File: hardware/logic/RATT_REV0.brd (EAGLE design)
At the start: 127 x 76.2 mm, 126 parts, among them IC1 TLP292-4, IC13 MCP73832, IC16 PCA9539PW, IC2 CPC1002N, IC200 TPS2115AIPWRQ1, IC3 CPC1002N, IC300 MAx98357, IC4 CPC1002N, IC5 CPC1002N, J1 4P-2.0, J2 4P-2.0, J4 4P-2.0, J5 F-1X04-SIP-100-40, J6 4P-2.0, J7 PHOENIX1803484, J8 PHOENIX1803484, Q5 2N7002, U1 RPI-ZERO, U5 AP2112K-3.3V

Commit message: Moved all parts into MakeItLabs Library
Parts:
- removed U5: AP2112K-3.3V, SparkFun-PowerIC:SOT23-5
- added IC500: AP2112K-3.3V, MakeItLabs:SOT23-5
- C1, C20, C23: device SparkFun-Capacitors:0805@1 -> MakeItLabs:0805-CAP
- C10, C19, C8: device SparkFun-Capacitors:0603 -> MakeItLabs:0603-CAP
- C18, C2, C22, C3: device SparkFun-Capacitors:0603-CAP@1 -> MakeItLabs:0603-CAP
- C7: device SparkFun-Capacitors:0805 -> MakeItLabs:0603-CAP
- D10, D2, D3, D5, D6, D7, D8, D9: device DURRIDGE-DIODES:SOT-23 -> MakeItLabs:SOT-23
- FB1, FB2: device Adafruit_MAX98357:0603 -> MakeItLabs:0603
- FB3, FB4: device DURRIDGE-INDUCTORS:0603 -> MakeItLabs:0603
- IC1: device DURRIDGE-IC:SO-16 -> MakeItLabs:SO-16
- IC13: device SparkFun-PowerIC:SOT23-5 -> MakeItLabs:SOT23-5
- IC16: device Texas Instruments_By_element14_Batch_1:SOP65P640X120-24N -> MakeItLabs:SOP65P640X120-24N
- IC200: device Texas Instruments_By_element14_Batch_1:SOP65P640X120-8N -> MakeItLabs:SOP65P640X120-8N
- IC300: value MAx98357 -> MAX98357; device Adafruit_MAX98357:QFN16_3MM -> MakeItLabs:QFN16_3MM
- J100, J200: device Adafruit_MAX98357:TERMBLOCK_1X2-3.5MM -> MakeItLabs:TERMBLOCK_1X2-3.5MM
- J5: device con-headers-jp:SIP-100-04-40 -> MakeItLabs:SIP-100-04-40
- JP1: device pinhead:2X08 -> MakeItLabs:2X08
- JP2: device SparkFun-Connectors:JST-2-PTH -> MakeItLabs:JST-2-PTH
- LED1, LED2: device SparkFun-LED:LED5MM -> MakeItLabs:LED5MM
- LED3, LED4, LED5, LED6: device SparkFun-LED:LED-0603 -> MakeItLabs:LED-0603
- Q5: device zetex:SOT-23 -> MakeItLabs:SOT-23
- R1: device SparkFun-Passives:0603-RES -> MakeItLabs:0603-RES
- R11, R12, R18, R19, R21, R24, R36, R56, R57, R60, R61: device SparkFun-Resistors:0603 -> MakeItLabs:0603-RES
- R14, R15, R16, R22: device DURRIDGE-RESISTORS:2512-RES -> MakeItLabs:2512-RES
- SW0, SW1, SW2, SW3: device MakeIt_Labs:ESWITCH320 -> MakeItLabs:ESWITCH320
- U1: device RPI-Zero:RASPBERRYPI_BASTELSTUBE_V13_RASPI_BOARD_B+_FULL -> MakeItLabs:RASPBERRYPI_BASTELSTUBE_V13_RASPI_BOARD_B+_FULL
- moved R60 146.9 mm to (-78.2, -10.4)
- moved C2 146.9 mm to (-78.2, -16.8)
- moved C3 146.9 mm to (-78.2, -19.8)
- moved R11 146.9 mm to (-75.2, -0.51)
- moved R12 146.9 mm to (-75.2, -3.81)
- moved R61 146.9 mm to (-78.2, -13.7)
- moved IC200 112.7 mm to (-76.2, -27.4)
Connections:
- net +3.3V: now also IC500.5; no longer U5.5
- net +5VB: now also IC500.1; no longer U5.1
- net GND: now also IC500.2; no longer U5.2
- net N$18: now also IC500.3; no longer U5.3
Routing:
- net N$33: track 4.84 -> 6.13 mm
- net N$34: track 4.27 -> 3.29 mm

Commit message: most stuff placed
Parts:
- moved R24 148.9 mm to (45.2, 38.6), turned to 180 degrees
- moved LED5 131.4 mm to (4.32, 51.3)
- moved R57 125.7 mm to (4.32, 48.5), turned to 90 degrees
- moved LED4 125.0 mm to (2.54, 51.3)
- moved R56 119.2 mm to (2.54, 48.5), turned to 90 degrees
- moved C10 119.1 mm to (41.9, 43.9), turned to 180 degrees
- moved R61 115.0 mm to (19.8, 46.5)
- moved LED3 107.3 mm to (6.10, 51.3)
- moved R21 106.9 mm to (6.10, 48.5), turned to 90 degrees
- moved IC200 106.8 mm to (7.37, 39.1), turned to 270 degrees
- moved C2 101.6 mm to (9.65, 34.3)
- moved C7 100.2 mm to (42.7, 39.4), turned to 270 degrees
- moved C3 99.8 mm to (5.59, 34.3), turned to 180 degrees
- moved R60 98.2 mm to (4.57, 42.4)
- moved LED6 98.2 mm to (6.10, 7.62)
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- renumbered U1 to J87
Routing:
- net +5VIN: track 0.00 -> 253.2 mm, vias 0 -> 1
- net +5VB: track 116.6 -> 237.8 mm, vias 8 -> 10
- net CHARGE_STATUS: track 0.00 -> 66.1 mm, vias 0 -> 2
- net SHUTDOWN: track 5.25 -> 50.5 mm, vias 0 -> 2
- net V_BATT: track 0.00 -> 30.5 mm
- net !PWR_LOSS: track 0.00 -> 17.2 mm
- net +3.3V: track 105.2 -> 116.1 mm
- net I2S_WS/LRCLK: track 11.8 -> 16.5 mm
- net I2S_BCK: track 42.6 -> 46.7 mm
- net 3V3: track 23.9 -> 26.9 mm
- net N$18: track 0.00 -> 2.08 mm
- net N$14: track 0.00 -> 1.69 mm
- net I2C_SDA: track 48.5 -> 46.9 mm
- net N$17: track 0.00 -> 1.55 mm
- net I2S_DOUT: track 10.7 -> 9.20 mm
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
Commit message: Added some stuff
Added clamps to RFID, added 1206 series resistor to LCD backlight
power in connector updated
lipo connector moved
played with cut away of plane
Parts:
- removed SJ4: JUMPER-PAD-2-NC_BY_TRACE, MakeItLabs:SOLDERJUMPER_10MIL
- added D1, D4: BAT54S, MakeItLabs:SOT-23
- added R10: 100R, MakeItLabs:0603-RES
- added R9: 10R, MakeItLabs:1206-RES
- J100: value (none) -> PHOENIX1803426; device MakeItLabs:TERMBLOCK_1X2-3.5MM -> MakeItLabs:1803426
- moved C22 34.2 mm to (67.6, 65.2), turned to 90 degrees
- moved C23 32.5 mm to (65.4, 65.3), turned to 90 degrees
- moved FB3 18.7 mm to (66.5, 71.4), turned to 270 degrees
- moved C1 7.90 mm to (48.8, 72.1), turned to 270 degrees
- moved R41 5.74 mm to (72.1, 66.6), turned to 270 degrees
- moved C25 5.65 mm to (50.6, 72.2), turned to 270 degrees
- moved JP2 4.89 mm to (10.7, 19.8), turned to 270 degrees
- moved FB4 4.44 mm to (46.7, 72.1), turned to 270 degrees
- moved R37 3.39 mm to (56.4, 67.6), turned to 90 degrees
- moved R25 2.90 mm to (61.0, 39.9), turned to 90 degrees
- moved R30 2.30 mm to (61.0, 43.2), turned to 270 degrees
- moved R20 2.30 mm to (57.9, 69.1)
- moved J5 1.78 mm to (56.9, 72.1)
- moved R36 1.02 mm to (26.7, 55.9)
- moved LED3 0.51 mm to (6.10, 51.8)
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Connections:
- removed net N$26: LCD3.15, LCD3.2, SJ4.1
- new net N$10: J5.4, R10.2
- new net N$9: LCD3.15, R9.2
- net +3.3V: now also LCD3.2, R9.1; no longer SJ4.2
- net +5VB: now also D1.2, D4.2
- net +5VIN: now also J100.2; no longer J100.1
- net GND: now also D1.1, D4.1, J100.1; no longer J100.2
- net RFID_RX: now also D4.3, R10.1; no longer J5.4
- net RFID_TX: now also D1.3
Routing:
- net +3.3V: track 116.1 -> 296.3 mm, vias 7 -> 17
- net N$26: track 36.2 -> 0.00 mm
- net +5VB: track 237.8 -> 269.6 mm, vias 10 -> 12
- net N$51: track 0.00 -> 24.6 mm
- net !I/O_RESET: track 34.7 -> 29.4 mm, vias 0 -> 2
- net LED0: track 35.6 -> 40.4 mm
- net N$10: track 0.00 -> 4.39 mm
- net +5VIN: track 253.2 -> 256.3 mm
- net CHARGE_STATUS: track 66.1 -> 69.1 mm
- net RFID_TX: track 70.8 -> 73.2 mm
- net I2C_SDA: track 46.9 -> 48.9 mm
- net N$9: track 0.00 -> 1.90 mm
- net LED1: track 39.9 -> 38.8 mm
- net !BUTTON0: track 20.8 -> 21.8 mm
- net !I/O_IRQ: track 32.4 -> 32.7 mm, vias 0 -> 2
- added copper zone on layer 1, net +5VB
- added copper zone on layer 1, net N$16
- removed copper zone on layer 1, net VIN

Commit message: moved stuff for Steve
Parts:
- removed J200: (no value), MakeItLabs:TERMBLOCK_1X2-3.5MM
- removed JP1: (no value), MakeItLabs:2X08
- removed SJ3: JUMPER-PAD-2-NC_BY_TRACE, MakeItLabs:SOLDERJUMPER_10MIL
- added J3: (no value), MakeItLabs:2X08_SHROUD
- added JP4: (no value), MakeItLabs:MOLEX-1X2
- moved J100 16.0 mm to (9.91, 5.33), turned to 0 degrees
- moved R18 7.12 mm to (5.84, 11.7), turned to 0 degrees
- moved C19 6.62 mm to (4.06, 20.6)
- moved C8 6.62 mm to (6.60, 20.6)
- moved LED6 6.62 mm to (6.60, 14.2)
- moved R19 6.62 mm to (3.81, 14.2)
- moved IC13 6.62 mm to (5.33, 17.5)
- moved R42 5.88 mm to (76.6, 9.49), turned to 0 degrees
- moved FB4 4.75 mm to (48.0, 67.6)
- moved R41 4.13 mm to (76.2, 65.9)
- moved LED2 3.18 mm to (72.4, 9.53), turned to 0 degrees
- moved LED1 3.17 mm to (72.4, 66.7), turned to 0 degrees
- moved C23 2.99 mm to (68.3, 66.0), turned to 0 degrees
- moved R20 2.62 mm to (56.6, 66.8)
- moved R37 2.54 mm to (54.4, 66.0), turned to 0 degrees
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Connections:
- removed net N$3: LCD3.1, SJ3.1
- net +3.3V: now also D1.2, D4.2, J3.8; no longer JP1.8
- net +5VB: no longer D1.2, D4.2
- net +5VIN: now also J3.4; no longer JP1.4
- net GND: now also J3.2, J3.6, LCD3.1; no longer JP1.2, JP1.6, SJ3.2
- net I2C_SCL: now also J3.15; no longer JP1.15
- net I2C_SDA: now also J3.13; no longer JP1.13
- net IN0P: now also J3.16; no longer JP1.16
- net IN1P: now also J3.14; no longer JP1.14
- net IN2P: now also J3.12; no longer JP1.12
- net IN3P: now also J3.10; no longer JP1.10
- net N$6: now also JP4.2; no longer J200.1
- net N$7: now also JP4.1; no longer J200.2
- net OUT0P: now also J3.1; no longer JP1.1
- net OUT1P: now also J3.3; no longer JP1.3
- net OUT2P: now also J3.5; no longer JP1.5
- net OUT3P: now also J3.7; no longer JP1.7
- net RFID_RX: now also J3.11; no longer JP1.11
- net RFID_TX: now also J3.9; no longer JP1.9
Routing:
- net CHARGE_STATUS: track 69.1 -> 51.9 mm
- net +5VIN: track 256.3 -> 240.0 mm, vias 1 -> 3
- net V_BATT: track 30.9 -> 23.3 mm
- net LED0: track 40.4 -> 33.5 mm
- net +5VB: track 269.6 -> 263.8 mm, vias 12 -> 13
- net GND: track 4.81 -> 9.24 mm, vias 0 -> 2
- net +3.3V: track 296.3 -> 292.7 mm, vias 17 -> 16
- net LCD_MOSI: track 16.5 -> 19.5 mm
- net N$51: track 24.6 -> 27.5 mm
- net 5V_RFID_TX: track 2.40 -> 5.22 mm
- net N$49: track 4.46 -> 2.21 mm
- net RFID_TX: track 73.2 -> 71.1 mm, vias 2 -> 1
- net LED1: track 38.8 -> 36.7 mm
- net N$3: track 2.08 -> 0.00 mm
- net RFID_RX: track 65.6 -> 63.9 mm
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- added copper zone on layer 16, net N$16
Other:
- board text added: "+"
- board text added: "-"

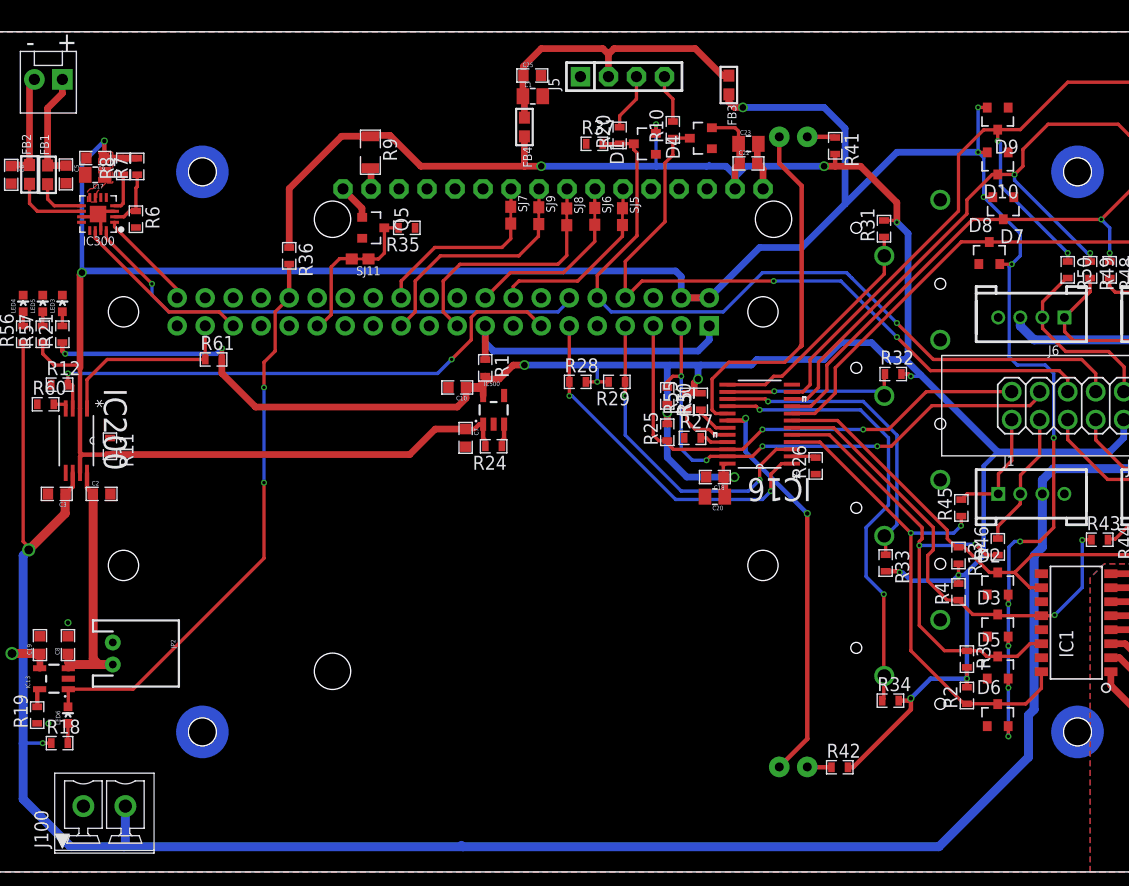
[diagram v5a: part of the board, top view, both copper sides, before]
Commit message: Added Test Points, GND Vias
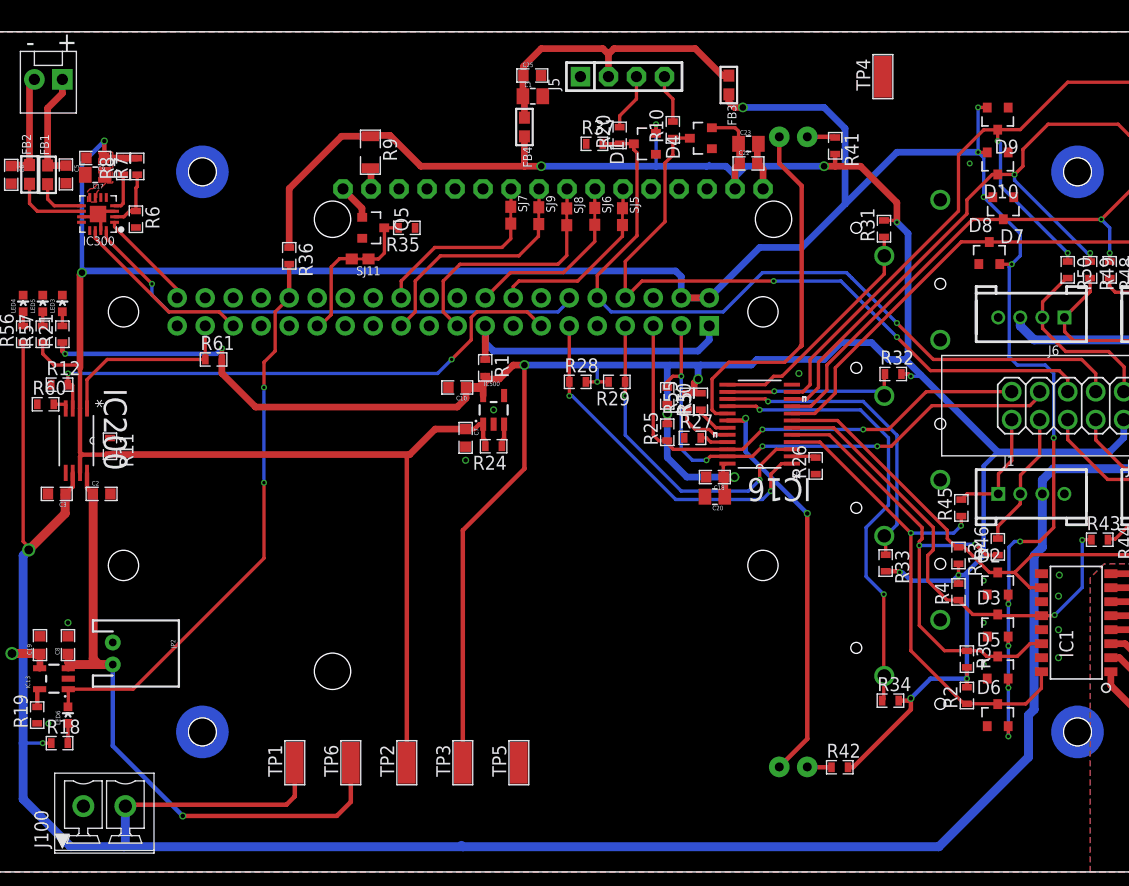
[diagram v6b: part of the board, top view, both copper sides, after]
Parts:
- added TP1: 5VIN, MakeItLabs:1206-RCW
- added TP2: 5VB, MakeItLabs:1206-RCW
- added TP3: 3.3V, MakeItLabs:1206-RCW
- added TP4, TP5: GND, MakeItLabs:1206-RCW
- added TP6: BATT, MakeItLabs:1206-RCW
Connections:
- net +3.3V: now also TP3.1
- net +5VB: now also TP2.1
- net +5VIN: now also TP1.1
- net GND: now also TP4.1, TP5.1
- net V_BATT: now also TP6.1
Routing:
- net +3.3V: track 292.7 -> 331.1 mm
- net V_BATT: track 23.3 -> 59.0 mm, vias 0 -> 1
- net +5VB: track 263.8 -> 291.9 mm
- net +5VIN: track 240.0 -> 258.8 mm
- net GND: vias 2 -> 13
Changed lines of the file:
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@@
 <element name="JP4" library="MakeItLabs" package="MOLEX-1X2" value="" x="6.096" y="71.882" rot="R180"/>
 <element name="J3" library="MakeItLabs" package="2X08_SHROUD" value="" x="101.092" y="42.291" rot="R180"/>
+<element name="TP1" library="MakeItLabs" package="1206-RCW" value="5VIN" x="27.178" y="9.906" rot="R90"/>
+<element name="TP2" library="MakeItLabs" package="1206-RCW" value="5VB" x="37.338" y="9.906" rot="R90"/>
+<element name="TP3" library="MakeItLabs" package="1206-RCW" value="3.3V" x="42.418" y="9.906" rot="R90"/>
+<element name="TP4" library="MakeItLabs" package="1206-RCW" value="GND" x="80.518" y="72.136" rot="R90"/>
+<element name="TP5" library="MakeItLabs" package="1206-RCW" value="GND" x="47.498" y="9.906" rot="R90"/>
+<element name="TP6" library="MakeItLabs" package="1206-RCW" value="BATT" x="32.258" y="9.906" rot="R90"/>
 </elements>
 <signals>
@@
 <via x="6.604" y="22.606" extent="1-16" drill="0.4"/>
 <via x="4.826" y="13.462" extent="1-16" drill="0.3"/>
+<contactref element="TP5" pad="1"/>
+<contactref element="TP4" pad="1"/>
+<via x="42.672" y="37.338" extent="1-16" drill="0.4"/>
+<via x="45.212" y="41.91" extent="1-16" drill="0.4"/>
+<via x="72.898" y="45.212" extent="1-16" drill="0.4"/>
+<via x="96.52" y="26.924" extent="1-16" drill="0.4"/>
+<via x="96.4438" y="25.019" extent="1-16" drill="0.4"/>
+<via x="96.4438" y="21.971" extent="1-16" drill="0.4"/>
+<via x="96.4438" y="19.431" extent="1-16" drill="0.4"/>
+<via x="89.662" y="26.416" extent="1-16" drill="0.3"/>
+<via x="89.662" y="22.606" extent="1-16" drill="0.3"/>
+<via x="89.662" y="18.796" extent="1-16" drill="0.3"/>
+<via x="88.392" y="64.262" extent="1-16" drill="0.3"/>
 </signal>
 <signal name="N$1">
@@
 <contactref element="R18" pad="2"/>
 <contactref element="LED6" pad="A"/>
-<wire x1="6.604" y1="13.474" x2="6.592" y2="11.684" width="0.3048" layer="1"/>
+<wire x1="6.604" y1="13.474" x2="6.604" y2="11.696" width="0.3048" layer="1"/>
+<wire x1="6.604" y1="11.696" x2="6.592" y2="11.684" width="0.3048" layer="1"/>
 </signal>
 <signal name="CHARGE_STATUS">
@@
 <wire x1="8.89" y1="34.252" x2="8.89" y2="19.32" width="0.8128" layer="1"/>
 <wire x1="8.89" y1="19.32" x2="9.398" y2="18.812" width="0.8128" layer="1"/>
+<contactref element="TP6" pad="1"/>
+<wire x1="10.668" y1="18.812" x2="10.668" y2="11.43" width="0.4064" layer="16"/>
+<wire x1="10.668" y1="11.43" x2="17.018" y2="5.08" width="0.4064" layer="16"/>
+<via x="17.018" y="5.08" extent="1-16" drill="0.4"/>
+<wire x1="17.018" y1="5.08" x2="30.988" y2="5.08" width="0.4064" layer="1"/>
+<wire x1="30.988" y1="5.08" x2="32.258" y2="6.35" width="0.4064" layer="1"/>
+<wire x1="32.258" y1="6.35" x2="32.258" y2="9.906" width="0.4064" layer="1"/>
 </signal>
 <signal name="N$11">
@@
 <wire x1="2.54" y1="29.972" x2="3.048" y2="29.464" width="0.3048" layer="1"/>
 <wire x1="3.048" y1="29.464" x2="3.048" y2="29.21" width="0.3048" layer="1"/>
+<contactref element="TP1" pad="1"/>
+<wire x1="27.178" y1="9.906" x2="27.178" y2="6.858" width="0.4064" layer="1"/>
+<wire x1="27.178" y1="6.858" x2="26.416" y2="6.096" width="0.4064" layer="1"/>
+<wire x1="26.416" y1="6.096" x2="11.938" y2="6.096" width="0.4064" layer="1"/>
+<wire x1="11.938" y1="6.096" x2="11.811" y2="5.969" width="0.4064" layer="1"/>
 </signal>
 <signal name="+5VB">
@@
 <wire x1="77.089" y1="67.437" x2="75.184" y2="69.342" width="0.6096" layer="16"/>
 <wire x1="75.184" y1="69.342" x2="67.818" y2="69.342" width="0.6096" layer="16"/>
+<contactref element="TP2" pad="1"/>
+<wire x1="37.338" y1="9.906" x2="37.338" y2="37.592" width="0.4064" layer="1"/>
+<wire x1="37.338" y1="37.592" x2="37.604" y2="37.858" width="0.4064" layer="1"/>
 </signal>
 <signal name="+3.3V">
@@
 <wire x1="64.008" y1="45.974" x2="68.58" y2="45.974" width="0.6096" layer="16"/>
 <wire x1="68.58" y1="45.974" x2="69.088" y2="46.482" width="0.6096" layer="16"/>
-<via x="60.96" y="41.656" extent="1-16" drill="0.6"/>
-<wire x1="60.96" y1="41.656" x2="60.96" y2="45.72" width="0.6096" layer="16"/>
+<via x="60.96" y="41.5544" extent="1-16" drill="0.6"/>
+<wire x1="60.96" y1="41.5544" x2="60.96" y2="45.72" width="0.6096" layer="16"/>
 <wire x1="60.96" y1="45.72" x2="61.214" y2="45.974" width="0.3048" layer="16"/>
 <wire x1="54.61" y1="44.45" x2="54.61" y2="45.974" width="0.3048" layer="16"/>
@@
 <wire x1="78.486" y1="64.008" x2="81.788" y2="60.706" width="0.6096" layer="1"/>
 <wire x1="81.788" y1="60.706" x2="81.788" y2="58.928" width="0.6096" layer="1"/>
-<wire x1="60.96" y1="40.628" x2="60.96" y2="41.656" width="0.6096" layer="1"/>
+<wire x1="60.96" y1="40.628" x2="60.96" y2="41.5544" width="0.6096" layer="1"/>
 <wire x1="63.40318125" y1="43.422" x2="63.40318125" y2="44.35318125" width="0.6096" layer="1"/>
 <wire x1="63.40318125" y1="44.35318125" x2="63.754" y2="44.704" width="0.6096" layer="1"/>
@@
 <wire x1="67.056" y1="35.814" x2="62.738" y2="35.814" width="0.6096" layer="16"/>
 <wire x1="62.738" y1="35.814" x2="60.96" y2="37.592" width="0.6096" layer="16"/>
-<wire x1="60.96" y1="37.592" x2="60.96" y2="41.656" width="0.6096" layer="16"/>
+<wire x1="60.96" y1="37.592" x2="60.96" y2="41.5544" width="0.6096" layer="16"/>
 <wire x1="26.67" y1="56.63" x2="26.67" y2="61.976" width="0.6096" layer="1"/>
 <wire x1="20.562" y1="46.482" x2="20.562" y2="45.224" width="0.6096" layer="1"/>
@@
 <wire x1="20.574" y1="47.498" x2="20.574" y2="46.494" width="0.4064" layer="1"/>
 <wire x1="20.574" y1="46.494" x2="20.562" y2="46.482" width="0.3048" layer="1"/>
-<wire x1="60.96" y1="41.656" x2="60.96" y2="42.43" width="0.3048" layer="1"/>
+<wire x1="60.96" y1="41.5544" x2="60.96" y2="42.43" width="0.6096" layer="1"/>
 <via x="49.53" y="64.008" extent="1-16" drill="0.6"/>
 <contactref element="R9" pad="1"/>
@@
 <wire x1="76.188" y1="65.112" x2="76.188" y2="64.02" width="0.4064" layer="1"/>
 <wire x1="76.188" y1="64.02" x2="76.2" y2="64.008" width="0.4064" layer="1"/>
+<contactref element="TP3" pad="1"/>
+<wire x1="42.418" y1="9.906" x2="42.418" y2="30.988" width="0.4064" layer="1"/>
+<wire x1="42.418" y1="30.988" x2="48.006" y2="36.576" width="0.4064" layer="1"/>
+<wire x1="48.006" y1="36.576" x2="48.006" y2="45.974" width="0.4064" layer="1"/>
 </signal>
 <signal name="N$37">
